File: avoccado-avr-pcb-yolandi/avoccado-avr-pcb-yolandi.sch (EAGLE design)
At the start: 49 parts, among them Q1 16MHz, Q2 FET, U2 MCP73831

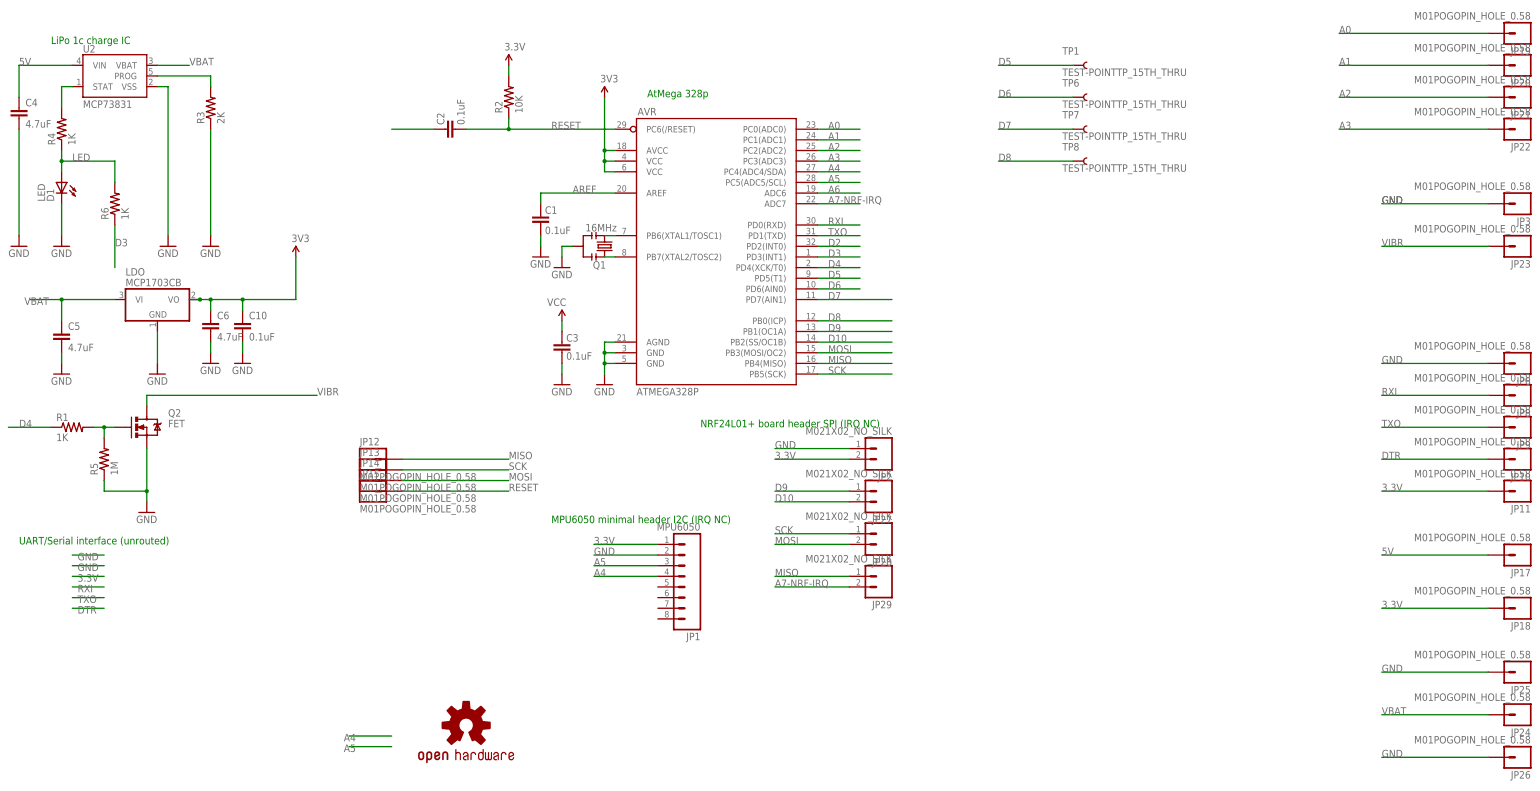
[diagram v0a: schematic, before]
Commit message: bottom silkscreen
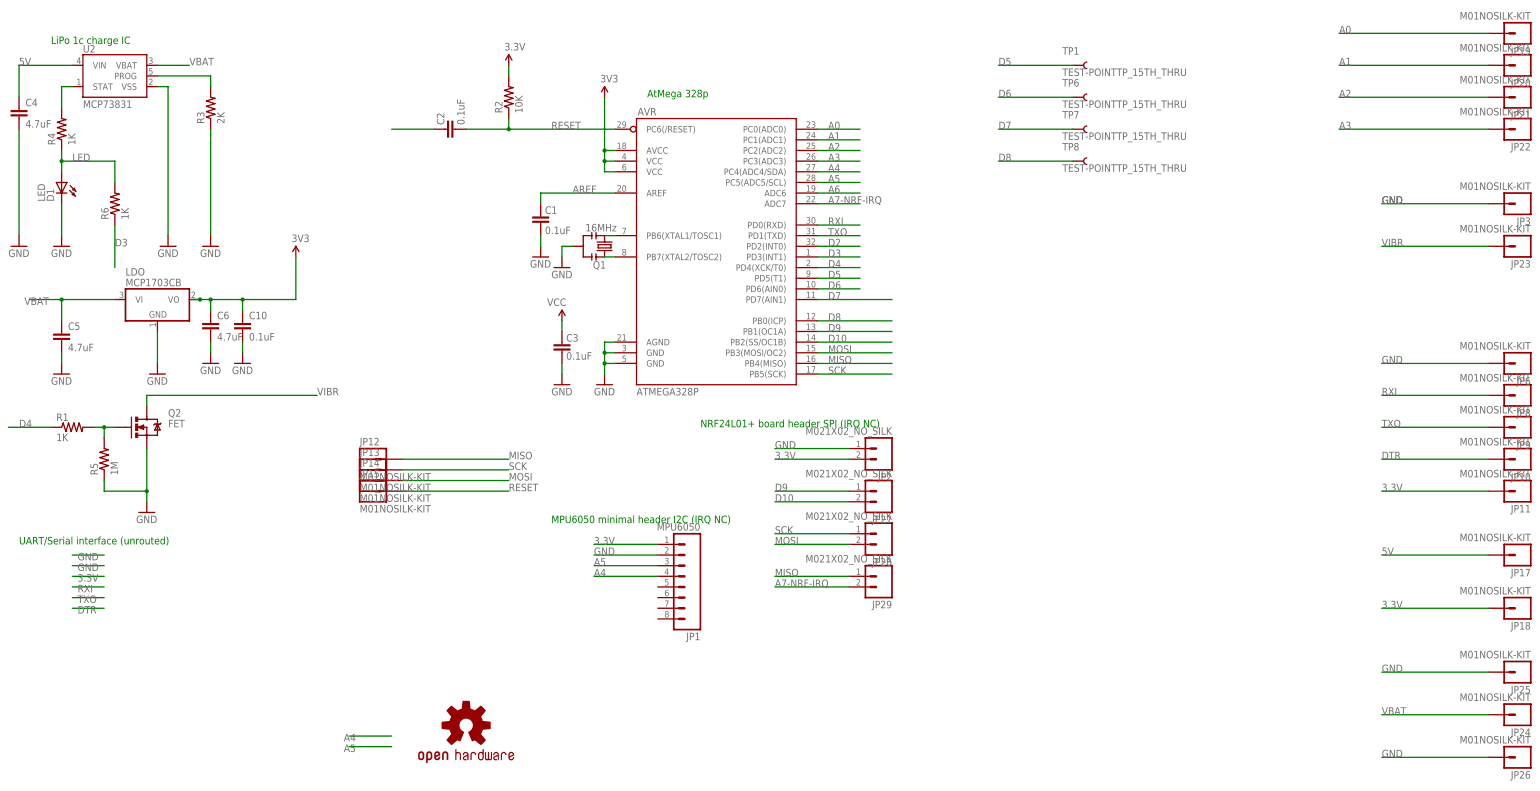
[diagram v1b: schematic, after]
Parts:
- JP10, JP11, JP12, JP13, JP14, JP15, JP17, JP18, JP19, JP20, JP21, JP22, JP23, JP24, JP25, JP26, JP3, JP6, JP8, JP9: value M01POGOPIN_HOLE_0.58 -> M01NOSILK-KIT; device SparkFun-Connectors:M01POGOPIN_HOLE_0.58 -> SparkFun-Connectors:M01NOSILK-KIT
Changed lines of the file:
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@@
 <part name="R6" library="SparkFun-Resistors" deviceset="RESISTOR" device="0603" value="1K"/>
 <part name="LOGO1" library="SparkFun-Aesthetics" deviceset="OSHW-LOGO" device="S"/>
-<part name="JP6" library="SparkFun-Connectors" deviceset="M01" device="POGOPIN_HOLE_0.58"/>
-<part name="JP8" library="SparkFun-Connectors" deviceset="M01" device="POGOPIN_HOLE_0.58"/>
-<part name="JP9" library="SparkFun-Connectors" deviceset="M01" device="POGOPIN_HOLE_0.58"/>
-<part name="JP10" library="SparkFun-Connectors" deviceset="M01" device="POGOPIN_HOLE_0.58"/>
-<part name="JP11" library="SparkFun-Connectors" deviceset="M01" device="POGOPIN_HOLE_0.58"/>
-<part name="JP12" library="SparkFun-Connectors" deviceset="M01" device="POGOPIN_HOLE_0.58"/>
-<part name="JP13" library="SparkFun-Connectors" deviceset="M01" device="POGOPIN_HOLE_0.58"/>
-<part name="JP14" library="SparkFun-Connectors" deviceset="M01" device="POGOPIN_HOLE_0.58"/>
-<part name="JP15" library="SparkFun-Connectors" deviceset="M01" device="POGOPIN_HOLE_0.58"/>
-<part name="JP3" library="SparkFun-Connectors" deviceset="M01" device="POGOPIN_HOLE_0.58"/>
-<part name="JP17" library="SparkFun-Connectors" deviceset="M01" device="POGOPIN_HOLE_0.58"/>
-<part name="JP18" library="SparkFun-Connectors" deviceset="M01" device="POGOPIN_HOLE_0.58"/>
+<part name="JP6" library="SparkFun-Connectors" deviceset="M01" device="NOSILK-KIT" value="M01NOSILK-KIT"/>
+<part name="JP8" library="SparkFun-Connectors" deviceset="M01" device="NOSILK-KIT" value="M01NOSILK-KIT"/>
+<part name="JP9" library="SparkFun-Connectors" deviceset="M01" device="NOSILK-KIT" value="M01NOSILK-KIT"/>
+<part name="JP10" library="SparkFun-Connectors" deviceset="M01" device="NOSILK-KIT" value="M01NOSILK-KIT"/>
+<part name="JP11" library="SparkFun-Connectors" deviceset="M01" device="NOSILK-KIT" value="M01NOSILK-KIT"/>
+<part name="JP12" library="SparkFun-Connectors" deviceset="M01" device="NOSILK-KIT" value="M01NOSILK-KIT"/>
+<part name="JP13" library="SparkFun-Connectors" deviceset="M01" device="NOSILK-KIT" value="M01NOSILK-KIT"/>
+<part name="JP14" library="SparkFun-Connectors" deviceset="M01" device="NOSILK-KIT" value="M01NOSILK-KIT"/>
+<part name="JP15" library="SparkFun-Connectors" deviceset="M01" device="NOSILK-KIT" value="M01NOSILK-KIT"/>
+<part name="JP3" library="SparkFun-Connectors" deviceset="M01" device="NOSILK-KIT" value="M01NOSILK-KIT"/>
+<part name="JP17" library="SparkFun-Connectors" deviceset="M01" device="NOSILK-KIT" value="M01NOSILK-KIT"/>
+<part name="JP18" library="SparkFun-Connectors" deviceset="M01" device="NOSILK-KIT" value="M01NOSILK-KIT"/>
 <part name="C2" library="SparkFun" deviceset="CAP" device="0402" value="0.1uF"/>
 <part name="TP1" library="SparkFun-Passives" deviceset="TEST-POINT" device="TP_15TH_THRU"/>
@@
 <part name="TP7" library="SparkFun-Passives" deviceset="TEST-POINT" device="TP_15TH_THRU"/>
 <part name="TP8" library="SparkFun-Passives" deviceset="TEST-POINT" device="TP_15TH_THRU"/>
-<part name="JP19" library="SparkFun-Connectors" deviceset="M01" device="POGOPIN_HOLE_0.58"/>
-<part name="JP20" library="SparkFun-Connectors" deviceset="M01" device="POGOPIN_HOLE_0.58"/>
-<part name="JP21" library="SparkFun-Connectors" deviceset="M01" device="POGOPIN_HOLE_0.58"/>
-<part name="JP22" library="SparkFun-Connectors" deviceset="M01" device="POGOPIN_HOLE_0.58"/>
+<part name="JP19" library="SparkFun-Connectors" deviceset="M01" device="NOSILK-KIT" value="M01NOSILK-KIT"/>
+<part name="JP20" library="SparkFun-Connectors" deviceset="M01" device="NOSILK-KIT" value="M01NOSILK-KIT"/>
+<part name="JP21" library="SparkFun-Connectors" deviceset="M01" device="NOSILK-KIT" value="M01NOSILK-KIT"/>
+<part name="JP22" library="SparkFun-Connectors" deviceset="M01" device="NOSILK-KIT" value="M01NOSILK-KIT"/>
 <part name="C5" library="SparkFun-Capacitors" deviceset="4.7UF-6.3V-10%(0603)" device="0603" value="4.7uF"/>
 <part name="C6" library="SparkFun-Capacitors" deviceset="4.7UF-6.3V-10%(0603)" device="0603" value="4.7uF"/>
-<part name="JP24" library="SparkFun-Connectors" deviceset="M01" device="POGOPIN_HOLE_0.58"/>
-<part name="JP23" library="SparkFun-Connectors" deviceset="M01" device="POGOPIN_HOLE_0.58"/>
-<part name="JP25" library="SparkFun-Connectors" deviceset="M01" device="POGOPIN_HOLE_0.58"/>
-<part name="JP26" library="SparkFun-Connectors" deviceset="M01" device="POGOPIN_HOLE_0.58"/>
+<part name="JP24" library="SparkFun-Connectors" deviceset="M01" device="NOSILK-KIT" value="M01NOSILK-KIT"/>
+<part name="JP23" library="SparkFun-Connectors" deviceset="M01" device="NOSILK-KIT" value="M01NOSILK-KIT"/>
+<part name="JP25" library="SparkFun-Connectors" deviceset="M01" device="NOSILK-KIT" value="M01NOSILK-KIT"/>
+<part name="JP26" library="SparkFun-Connectors" deviceset="M01" device="NOSILK-KIT" value="M01NOSILK-KIT"/>
 <part name="JP2" library="SparkFun-Connectors" deviceset="M02" device="1X02_NO_SILK"/>
 <part name="JP27" library="SparkFun-Connectors" deviceset="M02" device="1X02_NO_SILK"/>

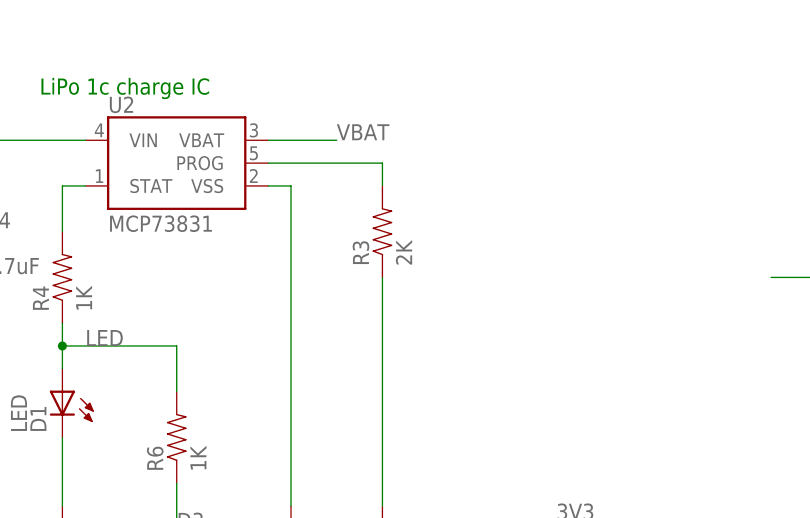
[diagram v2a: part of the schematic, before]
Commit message: silkscreen component values
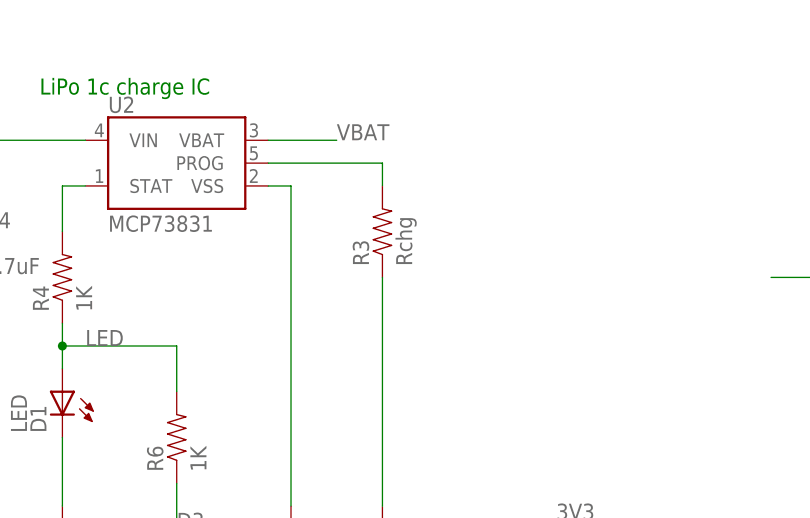
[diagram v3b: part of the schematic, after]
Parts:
- R3: value 2K -> Rchg
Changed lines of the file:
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@@
 <part name="U2" library="SparkFun" deviceset="MCP73831" device=""/>
 <part name="GND2" library="SparkFun" deviceset="GND" device=""/>
-<part name="R3" library="SparkFun-Resistors" deviceset="RESISTOR" device="0603" value="2K"/>
+<part name="R3" library="SparkFun-Resistors" deviceset="RESISTOR" device="0603" value="Rchg"/>
 <part name="GND3" library="SparkFun" deviceset="GND" device=""/>
 <part name="D1" library="SparkFun" deviceset="LED" device="0603" value="LED"/>
